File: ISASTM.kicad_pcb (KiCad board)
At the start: 4 copper layers, 101.6 x 101.6 mm, 137 parts, among them J1 Bus_ISA_8bit, J2 USB_C_Receptacle_USB2.0, J3 Boot select, J4 USB_C_Receptacle_USB2.0, J5 TagConnect_TC2030_SWD, SW1 Reset, U1 STM32H743IITx, U10 SN74AVC8T245PW, U11 SN74AVC8T245PW, U12 SN74AVC8T245PW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

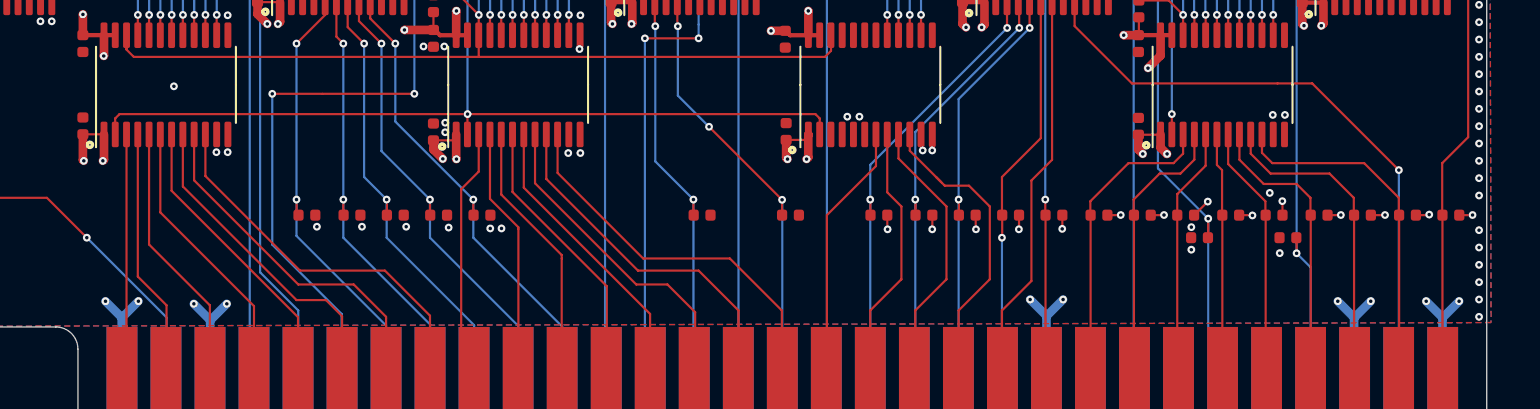
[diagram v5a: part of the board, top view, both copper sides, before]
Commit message: Add ISA signal labels
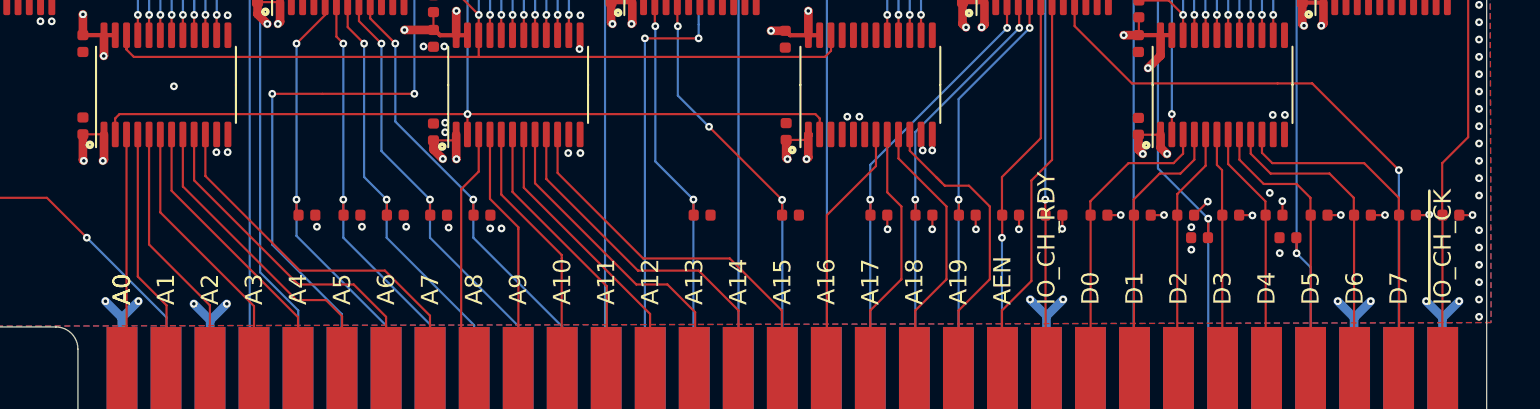
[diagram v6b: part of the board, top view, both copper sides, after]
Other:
- board text added: "+12V"
- board text added: "+5V"
- board text added: "-12V"
- board text added: "-5V"
- board text added: "A0"
- board text added: "A1"
- board text added: "A10"
- board text added: "A11"
- board text added: "A12"
- board text added: "A13"
- board text added: "A14"
- board text added: "A15"
- board text added: "A16"
- board text added: "A17"
- board text added: "A18"
- board text added: "A19"
- board text added: "A2"
- board text added: "A3"
- board text added: "A4"
- board text added: "A5"
- board text added: "A6"
- board text added: "A7"
- board text added: "A8"
- board text added: "A9"
- board text added: "AEN"
- board text added: "ALE"
- board text added: "CLK"
- board text added: "D0"
- board text added: "D1"
- board text added: "D2"
- board text added: "D3"
- board text added: "D4"
- board text added: "D5"
- board text added: "D6"
- board text added: "D7"
- board text added: "DRQ1"
- board text added: "DRQ2"
- board text added: "DRQ3"
- board text added: "GND"
- board text added: "IO_CH_RDY"
- board text added: "IRG5"
- board text added: "IRG7"
- board text added: "IRQ2"
- board text added: "IRQ3"
- board text added: "IRQ4"
- board text added: "IRQ6"
- board text added: "OSC"
- board text added: "RESET"
- board text added: "TC"
- board text added: "~DACK1"
- board text added: "~DACK2"
- board text added: "~DACK3"
- board text added: "~IOR"
- board text added: "~IOW"
- board text added: "~IO_CH_CK"
- board text added: "~NOWS"
- board text added: "~REFRESH"
- board text added: "~SMEMR"
- board text added: "~SMEMW"
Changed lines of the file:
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@@
   (general
     (thickness 1.6)
-    (drawings 35)
+    (drawings 98)
     (tracks 4971)
     (zones 0)
@@
     (pad_to_paste_clearance_ratio -0.1)
     (aux_axis_origin 0 0)
+    (grid_origin 38.1 112.4)
     (visible_elements FFFFFF7F)
     (pcbplotparams
@@
       (net 32 GND))
   )
+  (gr_text GND (at 114.3 107.32 90) (layer B.SilkS)
+    (effects (font (size 1 1) (thickness 0.15)) (justify right mirror))
+  )
+  (gr_text RESET (at 111.76 107.32 90) (layer B.SilkS)
+    (effects (font (size 1 1) (thickness 0.15)) (justify right mirror))
+  )
+  (gr_text +5V (at 109.22 107.32 90) (layer B.SilkS)
+    (effects (font (size 1 1) (thickness 0.15)) (justify right mirror))
+  )
+  (gr_text IRQ2 (at 106.68 107.32 90) (layer B.SilkS)
+    (effects (font (size 1 1) (thickness 0.15)) (justify right mirror))
+  )
+  (gr_text -5V (at 104.14 107.32 90) (layer B.SilkS)
+    (effects (font (size 1 1) (thickness 0.15)) (justify right mirror))
+  )
+  (gr_text DRQ2 (at 101.6 107.32 90) (layer B.SilkS)
+    (effects (font (size 1 1) (thickness 0.15)) (justify right mirror))
+  )
+  (gr_text -12V (at 99.06 107.32 90) (layer B.SilkS)
+    (effects (font (size 1 1) (thickness 0.15)) (justify right mirror))
+  )
+  (gr_text ~NOWS (at 96.52 107.32 90) (layer B.SilkS)
+    (effects (font (size 1 1) (thickness 0.15)) (justify right mirror))
+  )
+  (gr_text +12V (at 93.98 107.32 90) (layer B.SilkS)
+    (effects (font (size 1 1) (thickness 0.15)) (justify right mirror))
+  )
+  (gr_text GND (at 91.44 107.32 90) (layer B.SilkS)
+    (effects (font (size 1 1) (thickness 0.15)) (justify right mirror))
+  )
+  (gr_text ~SMEMW (at 88.9 107.32 90) (layer B.SilkS)
+    (effects (font (size 1 1) (thickness 0.15)) (justify right mirror))
+  )
+  (gr_text ~SMEMR (at 86.36 107.32 90) (layer B.SilkS)
+    (effects (font (size 1 1) (thickness 0.15)) (justify right mirror))
+  )
+  (gr_text ~IOW (at 83.82 107.32 90) (layer B.SilkS)
+    (effects (font (size 1 1) (thickness 0.15)) (justify right mirror))
+  )
+  (gr_text ~IOR (at 81.28 107.32 90) (layer B.SilkS)
+    (effects (font (size 1 1) (thickness 0.15)) (justify right mirror))
+  )
+  (gr_text ~DACK3 (at 78.74 107.32 90) (layer B.SilkS)
+    (effects (font (size 1 1) (thickness 0.15)) (justify right mirror))
+  )
+  (gr_text DRQ3 (at 76.2 107.32 90) (layer B.SilkS)
+    (effects (font (size 1 1) (thickness 0.15)) (justify right mirror))
+  )
+  (gr_text ~DACK1 (at 73.66 107.32 90) (layer B.SilkS)
+    (effects (font (size 1 1) (thickness 0.15)) (justify right mirror))
+  )
+  (gr_text DRQ1 (at 71.12 107.32 90) (layer B.SilkS)
+    (effects (font (size 1 1) (thickness 0.15)) (justify right mirror))
+  )
+  (gr_text ~REFRESH (at 68.58 107.32 90) (layer B.SilkS)
+    (effects (font (size 1 1) (thickness 0.15)) (justify right mirror))
+  )
+  (gr_text CLK (at 66.04 107.32 90) (layer B.SilkS)
+    (effects (font (size 1 1) (thickness 0.15)) (justify right mirror))
+  )
+  (gr_text IRG7 (at 63.5 107.32 90) (layer B.SilkS)
+    (effects (font (size 1 1) (thickness 0.15)) (justify right mirror))
+  )
+  (gr_text IRQ6 (at 60.96 107.32 90) (layer B.SilkS)
+    (effects (font (size 1 1) (thickness 0.15)) (justify right mirror))
+  )
+  (gr_text IRG5 (at 58.42 107.32 90) (layer B.SilkS)
+    (effects (font (size 1 1) (thickness 0.15)) (justify right mirror))
+  )
+  (gr_text IRQ4 (at 55.88 107.32 90) (layer B.SilkS)
+    (effects (font (size 1 1) (thickness 0.15)) (justify right mirror))
+  )
+  (gr_text IRQ3 (at 53.34 107.32 90) (layer B.SilkS)
+    (effects (font (size 1 1) (thickness 0.15)) (justify right mirror))
+  )
+  (gr_text ~DACK2 (at 50.8 107.32 90) (layer B.SilkS)
+    (effects (font (size 1 1) (thickness 0.15)) (justify right mirror))
+  )
+  (gr_text TC (at 48.26 107.32 90) (layer B.SilkS)
+    (effects (font (size 1 1) (thickness 0.15)) (justify right mirror))
+  )
+  (gr_text ALE (at 45.72 107.32 90) (layer B.SilkS)
+    (effects (font (size 1 1) (thickness 0.15)) (justify right mirror))
+  )
+  (gr_text +5V (at 43.18 107.32 90) (layer B.SilkS)
+    (effects (font (size 1 1) (thickness 0.15)) (justify right mirror))
+  )
+  (gr_text OSC (at 40.64 107.32 90) (layer B.SilkS)
+    (effects (font (size 1 1) (thickness 0.15)) (justify right mirror))
+  )
+  (gr_text A0 (at 38.1 107.32 90) (layer F.SilkS)
+    (effects (font (size 1 1) (thickness 0.15)) (justify left))
+  )
+  (gr_text GND (at 38.1 107.32 90) (layer B.SilkS)
+    (effects (font (size 1 1) (thickness 0.15)) (justify right mirror))
+  )
+  (gr_text ~IO_CH_CK (at 114.3 107.32 90) (layer F.SilkS)
+    (effects (font (size 1 1) (thickness 0.15)) (justify left))
+  )
+  (gr_text D7 (at 111.76 107.32 90) (layer F.SilkS)
+    (effects (font (size 1 1) (thickness 0.15)) (justify left))
+  )
+  (gr_text D6 (at 109.22 107.32 90) (layer F.SilkS)
+    (effects (font (size 1 1) (thickness 0.15)) (justify left))
+  )
+  (gr_text D5 (at 106.68 107.32 90) (layer F.SilkS)
+    (effects (font (size 1 1) (thickness 0.15)) (justify left))
+  )
+  (gr_text D4 (at 104.14 107.32 90) (layer F.SilkS)
+    (effects (font (size 1 1) (thickness 0.15)) (justify left))
+  )
+  (gr_text D3 (at 101.6 107.32 90) (layer F.SilkS)
+    (effects (font (size 1 1) (thickness 0.15)) (justify left))
+  )
+  (gr_text D2 (at 99.06 107.32 90) (layer F.SilkS)
+    (effects (font (size 1 1) (thickness 0.15)) (justify left))
+  )
+  (gr_text D1 (at 96.52 107.32 90) (layer F.SilkS)
+    (effects (font (size 1 1) (thickness 0.15)) (justify left))
+  )
+  (gr_text D0 (at 93.98 107.32 90) (layer F.SilkS)
+    (effects (font (size 1 1) (thickness 0.15)) (justify left))
+  )
+  (gr_text IO_CH_RDY (at 91.44 107.32 90) (layer F.SilkS)
+    (effects (font (size 1 1) (thickness 0.15)) (justify left))
+  )
+  (gr_text AEN (at 88.9 107.32 90) (layer F.SilkS)
+    (effects (font (size 1 1) (thickness 0.15)) (justify left))
+  )
+  (gr_text A19 (at 86.36 107.32 90) (layer F.SilkS)
+    (effects (font (size 1 1) (thickness 0.15)) (justify left))
+  )
+  (gr_text A18 (at 83.82 107.32 90) (layer F.SilkS)
+    (effects (font (size 1 1) (thickness 0.15)) (justify left))
+  )
+  (gr_text A17 (at 81.28 107.32 90) (layer F.SilkS)
+    (effects (font (size 1 1) (thickness 0.15)) (justify left))
+  )
+  (gr_text A16 (at 78.74 107.32 90) (layer F.SilkS)
+    (effects (font (size 1 1) (thickness 0.15)) (justify left))
+  )
+  (gr_text A15 (at 76.2 107.32 90) (layer F.SilkS)
+    (effects (font (size 1 1) (thickness 0.15)) (justify left))
+  )
+  (gr_text A14 (at 73.66 107.32 90) (layer F.SilkS)
+    (effects (font (size 1 1) (thickness 0.15)) (justify left))
+  )
+  (gr_text A13 (at 71.12 107.32 90) (layer F.SilkS)
+    (effects (font (size 1 1) (thickness 0.15)) (justify left))
+  )
+  (gr_text A12 (at 68.58 107.32 90) (layer F.SilkS)
+    (effects (font (size 1 1) (thickness 0.15)) (justify left))
+  )
+  (gr_text A11 (at 66.04 107.32 90) (layer F.SilkS)
+    (effects (font (size 1 1) (thickness 0.15)) (justify left))
+  )
+  (gr_text A10 (at 63.5 107.32 90) (layer F.SilkS)
+    (effects (font (size 1 1) (thickness 0.15)) (justify left))
+  )
+  (gr_text A9 (at 60.96 107.32 90) (layer F.SilkS)
+    (effects (font (size 1 1) (thickness 0.15)) (justify left))
+  )
+  (gr_text A8 (at 58.42 107.32 90) (layer F.SilkS)
+    (effects (font (size 1 1) (thickness 0.15)) (justify left))
+  )
+  (gr_text A7 (at 55.88 107.32 90) (layer F.SilkS)
+    (effects (font (size 1 1) (thickness 0.15)) (justify left))
+  )
+  (gr_text A6 (at 53.34 107.32 90) (layer F.SilkS)
+    (effects (font (size 1 1) (thickness 0.15)) (justify left))
+  )
+  (gr_text A5 (at 50.8 107.32 90) (layer F.SilkS)
+    (effects (font (size 1 1) (thickness 0.15)) (justify left))
+  )
+  (gr_text A4 (at 48.26 107.32 90) (layer F.SilkS)
+    (effects (font (size 1 1) (thickness 0.15)) (justify left))
+  )
+  (gr_text A3 (at 45.72 107.32 90) (layer F.SilkS)
+    (effects (font (size 1 1) (thickness 0.15)) (justify left))
+  )
+  (gr_text A2 (at 43.18 107.32 90) (layer F.SilkS)
+    (effects (font (size 1 1) (thickness 0.15)) (justify left))
+  )
+  (gr_text A1 (at 40.64 107.32 90) (layer F.SilkS)
+    (effects (font (size 1 1) (thickness 0.15)) (justify left))
+  )
+  (gr_text A0 (at 38.1 107.32 90) (layer F.SilkS)
+    (effects (font (size 1 1) (thickness 0.15)) (justify left))
+  )
   (gr_circle (center 115.075 30.7) (end 115.075 30.8) (layer F.SilkS) (width 0.3))
